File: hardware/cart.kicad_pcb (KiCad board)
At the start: 2 copper layers, 83.7 x 42 mm, 34 parts, among them J4 debug-snoop, P1 edge connector, U1 74LVC138A, U2 MCP1827S-3302E/EB, U3 74LVC8T245, U4 74LVC8T245, U5 74LVC8T245, U6 S29AL016J55TFIR20, U7 74LVC8T245, U8 74LVC8T245

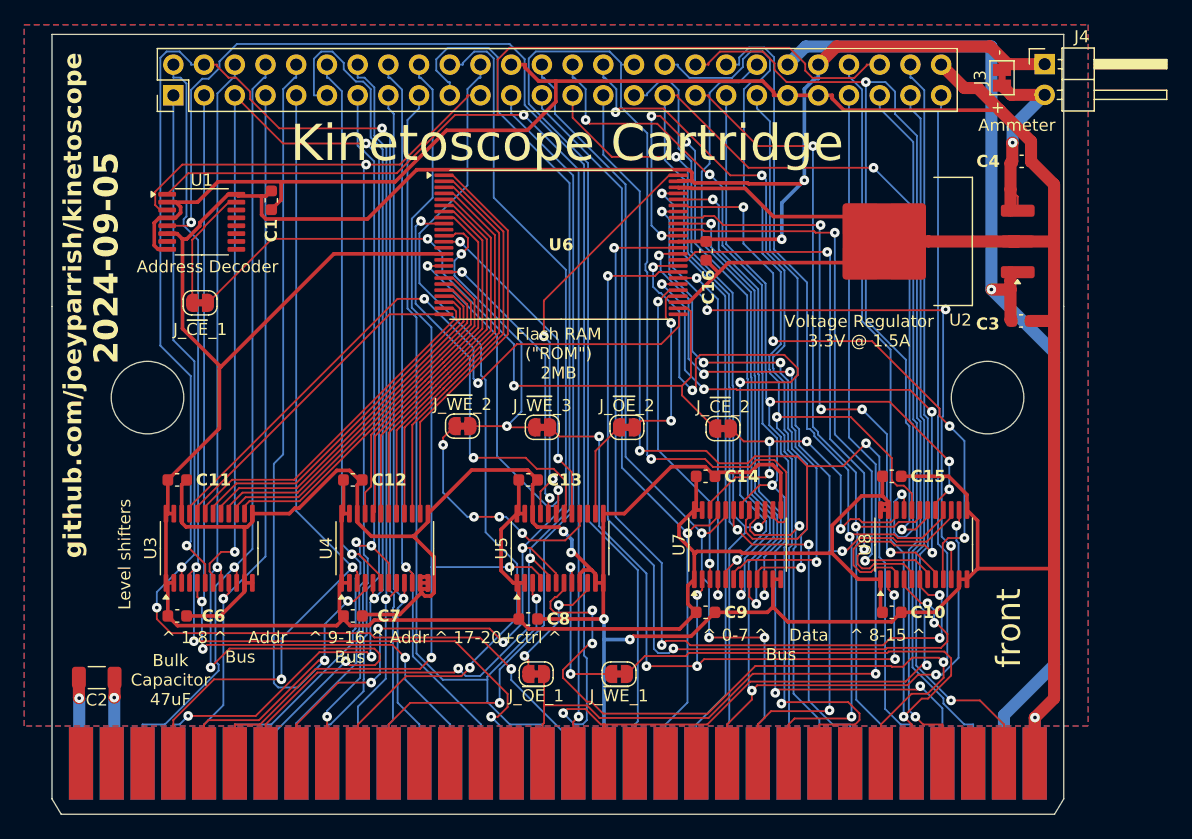
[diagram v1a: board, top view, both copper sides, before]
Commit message: Reannotate schematics and drop debug bridges
Parts are now numbered starting at 0 for cart, 100 for SRAM, 300 for
microcontroller.

Also, drop debug bridges that made routing more difficult and had the
same names across prototype boards.

Hopefully this will help avoid naming conflicts for the unified PCB.

Also, redo prototype PCB layouts.

Now that all the names have changed, update board layouts.
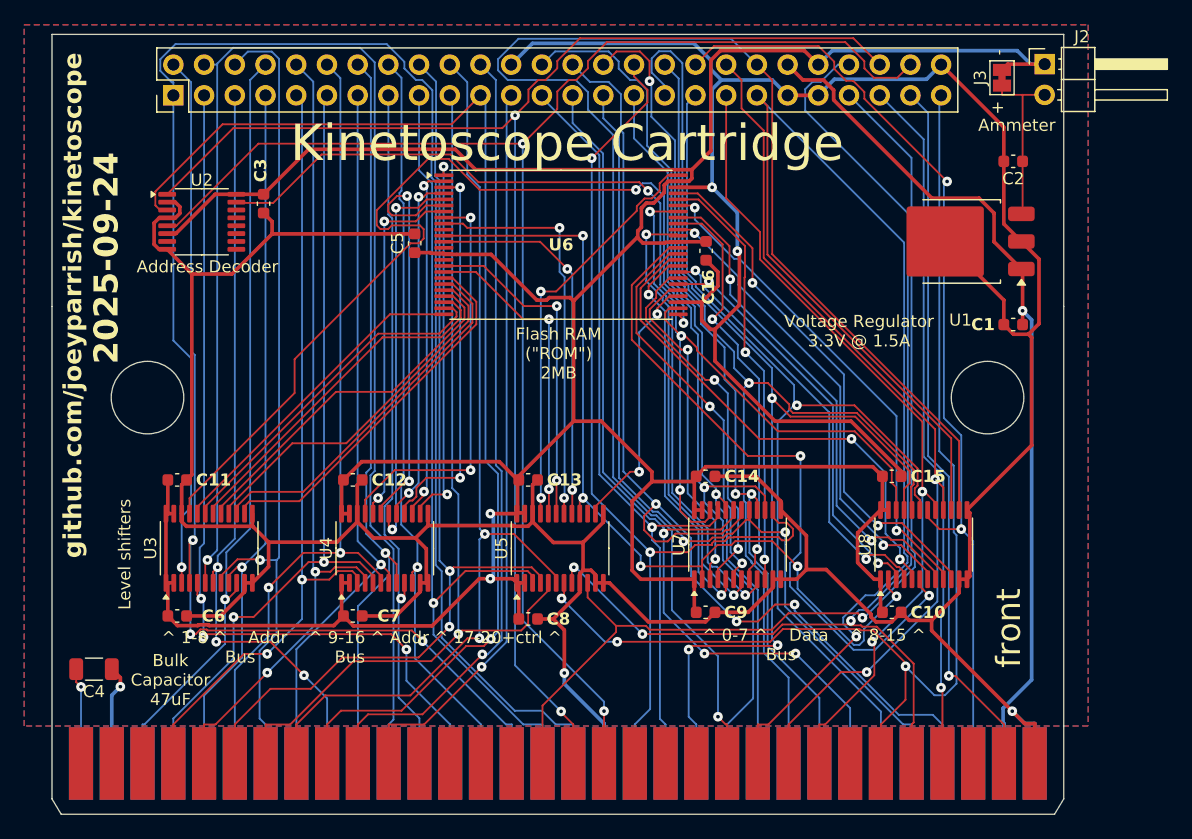
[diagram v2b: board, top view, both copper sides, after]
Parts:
- removed J_~{CE}_1, J_~{CE}_2, J_~{OE}_1, J_~{OE}_2, J_~{WE}_1, J_~{WE}_2, J_~{WE}_3: ~, Jumper:SolderJumper-2_P1.3mm_Bridged_RoundedPad1.0x1.5mm
- added C5: 22nF, Capacitor_SMD:C_0603_1608Metric, F.Cu at (43.0, 30.8)
- C1: value 22nF -> 4.7uF
- C2: value 47uF -> 1uF; footprint Capacitor_SMD:C_1206_3216Metric -> Capacitor_SMD:C_0603_1608Metric
- C3: value 4.7uF -> 22nF
- C4: value 1uF -> 47uF; footprint Capacitor_SMD:C_0603_1608Metric -> Capacitor_SMD:C_1206_3216Metric
- moved C4 87.5 mm to (16.5, 66.0), turned to 180 degrees
- moved C2 87.0 mm to (92.5, 24.0)
- moved C3 63.4 mm to (30.5, 27.5), turned to -90 degrees
- moved C1 62.2 mm to (92.5, 37.5), turned to 180 degrees
- renumbered J4 to J2, U2 to U1, U1 to U2
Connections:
- net /SEGA_A1 renamed SEGA_A1
- net /SEGA_A10 renamed SEGA_A10
- net /SEGA_A11 renamed SEGA_A11
- net /SEGA_A12 renamed SEGA_A12
- net /SEGA_A13 renamed SEGA_A13
- net /SEGA_A14 renamed SEGA_A14
- net /SEGA_A15 renamed SEGA_A15
- net /SEGA_A16 renamed SEGA_A16
- net /SEGA_A17 renamed SEGA_A17
- net /SEGA_A18 renamed SEGA_A18
- net /SEGA_A19 renamed SEGA_A19
- net /SEGA_A2 renamed SEGA_A2
- net /SEGA_A20 renamed SEGA_A20
- net /SEGA_A21 renamed SEGA_A21
- net /SEGA_A22 renamed SEGA_A22
- net /SEGA_A23 renamed SEGA_A23
- net /SEGA_A3 renamed SEGA_A3
- net /SEGA_A4 renamed SEGA_A4
- net /SEGA_A5 renamed SEGA_A5
- net /SEGA_A6 renamed SEGA_A6
- net /SEGA_A7 renamed SEGA_A7
- net /SEGA_A8 renamed SEGA_A8
- net /SEGA_A9 renamed SEGA_A9
- net /SEGA_D0 renamed SEGA_D0
- net /SEGA_D1 renamed SEGA_D1
- net /SEGA_D10 renamed SEGA_D10
- net /SEGA_D11 renamed SEGA_D11
- net /SEGA_D12 renamed SEGA_D12
- net /SEGA_D13 renamed SEGA_D13
- net /SEGA_D14 renamed SEGA_D14
- net /SEGA_D15 renamed SEGA_D15
- net /SEGA_D2 renamed SEGA_D2
- net /SEGA_D3 renamed SEGA_D3
- net /SEGA_D4 renamed SEGA_D4
- net /SEGA_D5 renamed SEGA_D5
- net /SEGA_D6 renamed SEGA_D6
- net /SEGA_D7 renamed SEGA_D7
- net /SEGA_D8 renamed SEGA_D8
- net /SEGA_D9 renamed SEGA_D9
- net /flash-internal/A0_3V renamed /cart-internal/flash-internal/A0_3V
- net /flash-internal/A10_3V renamed /cart-internal/flash-internal/A10_3V
- net /flash-internal/A11_3V renamed /cart-internal/flash-internal/A11_3V
- net /flash-internal/A12_3V renamed /cart-internal/flash-internal/A12_3V
- net /flash-internal/A13_3V renamed /cart-internal/flash-internal/A13_3V
- net /flash-internal/A14_3V renamed /cart-internal/flash-internal/A14_3V
- net /flash-internal/A15_3V renamed /cart-internal/flash-internal/A15_3V
- net /flash-internal/A16_3V renamed /cart-internal/flash-internal/A16_3V
- net /flash-internal/A17_3V renamed /cart-internal/flash-internal/A17_3V
- net /flash-internal/A18_3V renamed /cart-internal/flash-internal/A18_3V
- net /flash-internal/A19_3V renamed /cart-internal/flash-internal/A19_3V
- net /flash-internal/A1_3V renamed /cart-internal/flash-internal/A1_3V
- net /flash-internal/A2_3V renamed /cart-internal/flash-internal/A2_3V
- net /flash-internal/A3_3V renamed /cart-internal/flash-internal/A3_3V
- net /flash-internal/A4_3V renamed /cart-internal/flash-internal/A4_3V
- net /flash-internal/A5_3V renamed /cart-internal/flash-internal/A5_3V
- net /flash-internal/A6_3V renamed /cart-internal/flash-internal/A6_3V
- net /flash-internal/A7_3V renamed /cart-internal/flash-internal/A7_3V
- net /flash-internal/A8_3V renamed /cart-internal/flash-internal/A8_3V
- net /flash-internal/A9_3V renamed /cart-internal/flash-internal/A9_3V
- net /flash-internal/D0_3V renamed /cart-internal/flash-internal/D0_3V
- net /flash-internal/D10_3V renamed /cart-internal/flash-internal/D10_3V
- net /flash-internal/D11_3V renamed /cart-internal/flash-internal/D11_3V
- net /flash-internal/D12_3V renamed /cart-internal/flash-internal/D12_3V
- net /flash-internal/D13_3V renamed /cart-internal/flash-internal/D13_3V
- net /flash-internal/D14_3V renamed /cart-internal/flash-internal/D14_3V
- net /flash-internal/D15_3V renamed /cart-internal/flash-internal/D15_3V
- net /flash-internal/D1_3V renamed /cart-internal/flash-internal/D1_3V
- net /flash-internal/D2_3V renamed /cart-internal/flash-internal/D2_3V
- net /flash-internal/D3_3V renamed /cart-internal/flash-internal/D3_3V
- net /flash-internal/D4_3V renamed /cart-internal/flash-internal/D4_3V
- net /flash-internal/D5_3V renamed /cart-internal/flash-internal/D5_3V
- net /flash-internal/D6_3V renamed /cart-internal/flash-internal/D6_3V
- net /flash-internal/D7_3V renamed /cart-internal/flash-internal/D7_3V
- net /flash-internal/D8_3V renamed /cart-internal/flash-internal/D8_3V
- net /flash-internal/D9_3V renamed /cart-internal/flash-internal/D9_3V
- net /flash-internal/~{RESET_3V} renamed /cart-internal/flash-internal/~{RESET_3V}
- net /~{SEGA_AS} renamed ~{SEGA_AS}
- net /~{SEGA_CE} renamed ~{SEGA_CE}
- net /~{SEGA_REGISTER} renamed ~{SEGA_REGISTER}
- net /~{SEGA_RESET} renamed ~{SEGA_RESET}
- net /~{SEGA_WE_UB} renamed ~{SEGA_WE_UB}
- C1 pad 1: +3.3V -> +5V
- C2 pad 1: +5VP -> /cart-internal/+3.3V_INT
- C2 pad 2: GNDPWR -> GND
- C3 pad 1: +5V -> +3.3V
- C4 pad 1: /+3.3V_INT -> +5VP
- C4 pad 2: GND -> GNDPWR
- J1 pad 45: /~{SEGA_OE} -> ~{SEGA_OE}
- J1 pad 46: /~{SEGA_WE_LB} -> ~{SEGA_WE_LB}
- J2 pad 2: /+3.3V_INT -> /cart-internal/+3.3V_INT
- J3 pad 1: /+3.3V_INT -> /cart-internal/+3.3V_INT
- P1 pad B16: /~{SEGA_OE} -> ~{SEGA_OE}
- P1 pad B28: /~{SEGA_WE_LB} -> ~{SEGA_WE_LB}
- U1 pad 3: /+3.3V_INT -> /cart-internal/+3.3V_INT
- U2 pad 15: /~{FLASH_CE} -> /cart-internal/~{FLASH_CE}
- U5 pad 10: /flash-internal/~{OE_INT} -> ~{SEGA_OE}
- U5 pad 14: /flash-internal/~{OE_3V} -> /cart-internal/flash-internal/~{OE_3V}
- U5 pad 16: /flash-internal/~{WE_3V} -> /cart-internal/flash-internal/~{WE_3V}
- U5 pad 8: /flash-internal/~{WE_INT} -> ~{SEGA_WE_LB}
- U6 pad 11: /flash-internal/~{WE_3V_INT} -> /cart-internal/flash-internal/~{WE_3V}
- U6 pad 26: /flash-internal/~{CE_3V_INT} -> /cart-internal/~{FLASH_CE}
- U6 pad 28: /flash-internal/~{OE_3V_INT} -> /cart-internal/flash-internal/~{OE_3V}
- U7 pad 2: /flash-internal/DATA_DIR_INT -> /cart-internal/flash-internal/~{WE_3V}
- U7 pad 22: /flash-internal/~{DATA_OE_INT} -> /cart-internal/~{FLASH_CE}
- U8 pad 2: /flash-internal/DATA_DIR_INT -> /cart-internal/flash-internal/~{WE_3V}
- U8 pad 22: /flash-internal/~{DATA_OE_INT} -> /cart-internal/~{FLASH_CE}
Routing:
- net /cart-internal/~{FLASH_CE}: track 0.00 -> 97.6 mm, vias 0 -> 3
- net ~{SEGA_WE_LB}: track 0.00 -> 96.5 mm, vias 0 -> 3
- net /~{SEGA_WE_LB}: track 94.6 -> 0.00 mm, vias 1 -> 0
- net ~{SEGA_OE}: track 0.00 -> 87.0 mm, vias 0 -> 1
- net /~{SEGA_OE}: track 85.6 -> 0.00 mm, vias 1 -> 0
- net /cart-internal/flash-internal/~{WE_3V}: track 0.00 -> 74.2 mm, vias 0 -> 5
- net ~{SEGA_AS}: track 189.2 -> 125.0 mm, vias 3 -> 2
- net /flash-internal/~{CE_3V_INT}: track 61.7 -> 0.00 mm, vias 2 -> 0
- net /flash-internal/DATA_DIR_INT: track 60.0 -> 0.00 mm, vias 6 -> 0
- net SEGA_A1: track 87.6 -> 132.4 mm, vias 3 -> 1
- net SEGA_D7: track 123.4 -> 78.6 mm, vias 1 -> 2
- net SEGA_A5: track 108.1 -> 63.8 mm, vias 2 -> 3
- net SEGA_D15: track 95.5 -> 136.5 mm, vias 3 -> 1
- net SEGA_D11: track 119.9 -> 79.8 mm
- net /cart-internal/flash-internal/D9_3V: track 70.3 -> 35.7 mm, vias 4 -> 2
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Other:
- board text added: "2025-09-24"
- board text removed: "2024-09-05"
